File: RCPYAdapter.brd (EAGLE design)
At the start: 39.9 x 34.5 mm, 3 parts, among them X1 FCI_88400_066LF_RJ12_4POS, X2 FCI_88400_066LF_RJ12_4POS, X3 FCI_88400_066LF_RJ12_4POS

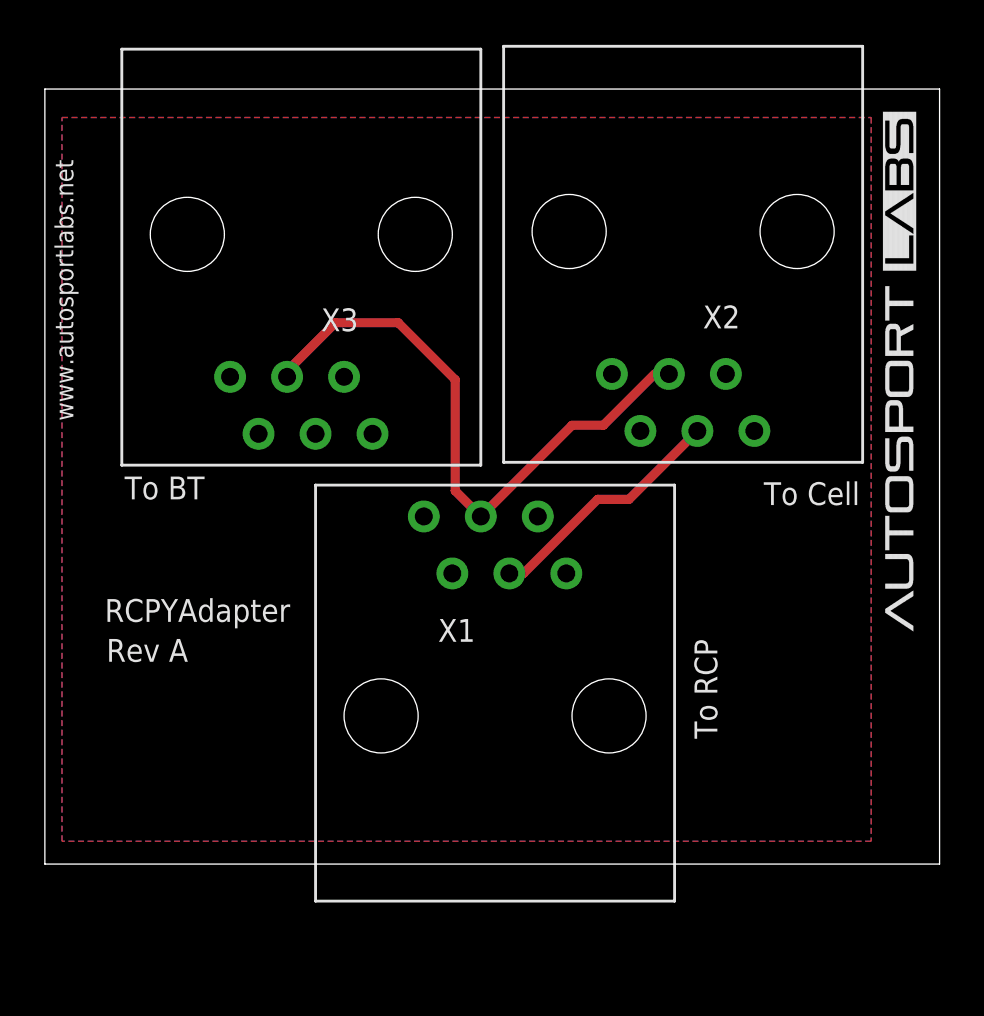
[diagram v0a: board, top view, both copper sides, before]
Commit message: corrected inverted Y adapter traces, resized board for standard size
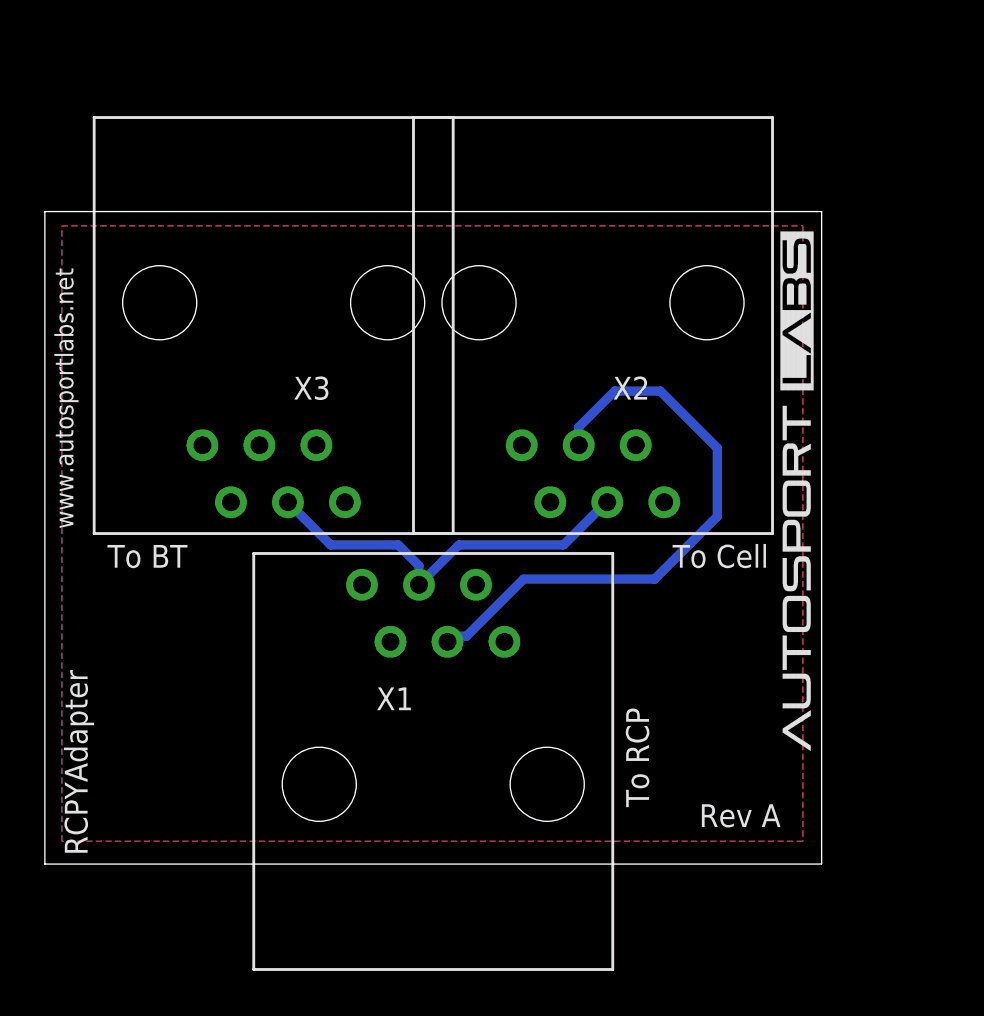
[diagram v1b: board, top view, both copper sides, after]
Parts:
- moved X2 5.12 mm to (24.4, 25.0)
- moved X1 4.11 mm to (17.3, 3.56)
- moved X3 3.29 mm to (10.2, 25.0)
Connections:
- net RXD0_JACK: now also X2.P4; no longer X2.P3
- net TXD0_JACK: now also X2.P3, X3.P3; no longer X2.P4, X3.P4
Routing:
- net RXD0_JACK: track 11.0 -> 26.1 mm
- net TXD0_JACK: track 27.1 -> 17.8 mm
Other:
- board size 39.9 x 34.5 mm -> 34.6 x 29.1 mm
